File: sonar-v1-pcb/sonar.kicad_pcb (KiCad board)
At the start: 2 copper layers, 189 parts, among them U1 AD7606, U10 AD7606, U19 AD7606

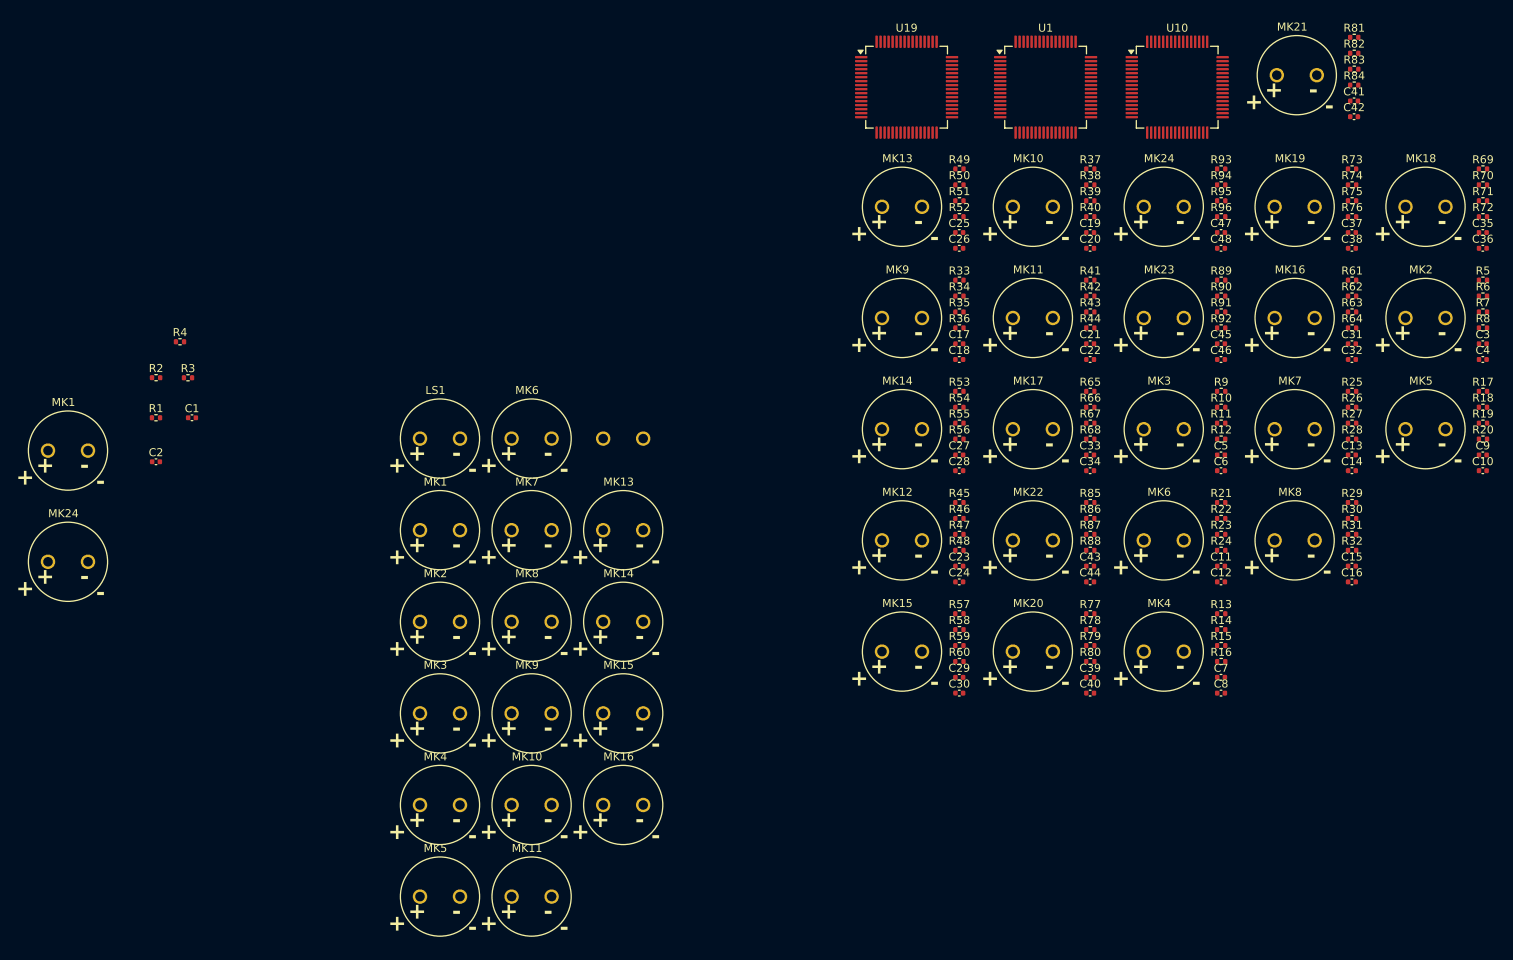
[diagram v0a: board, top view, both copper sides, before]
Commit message: Update gitignore and save schematic/PCB progress
Co-Authored-By: Claude Opus 4.6 <noreply@anthropic.com>
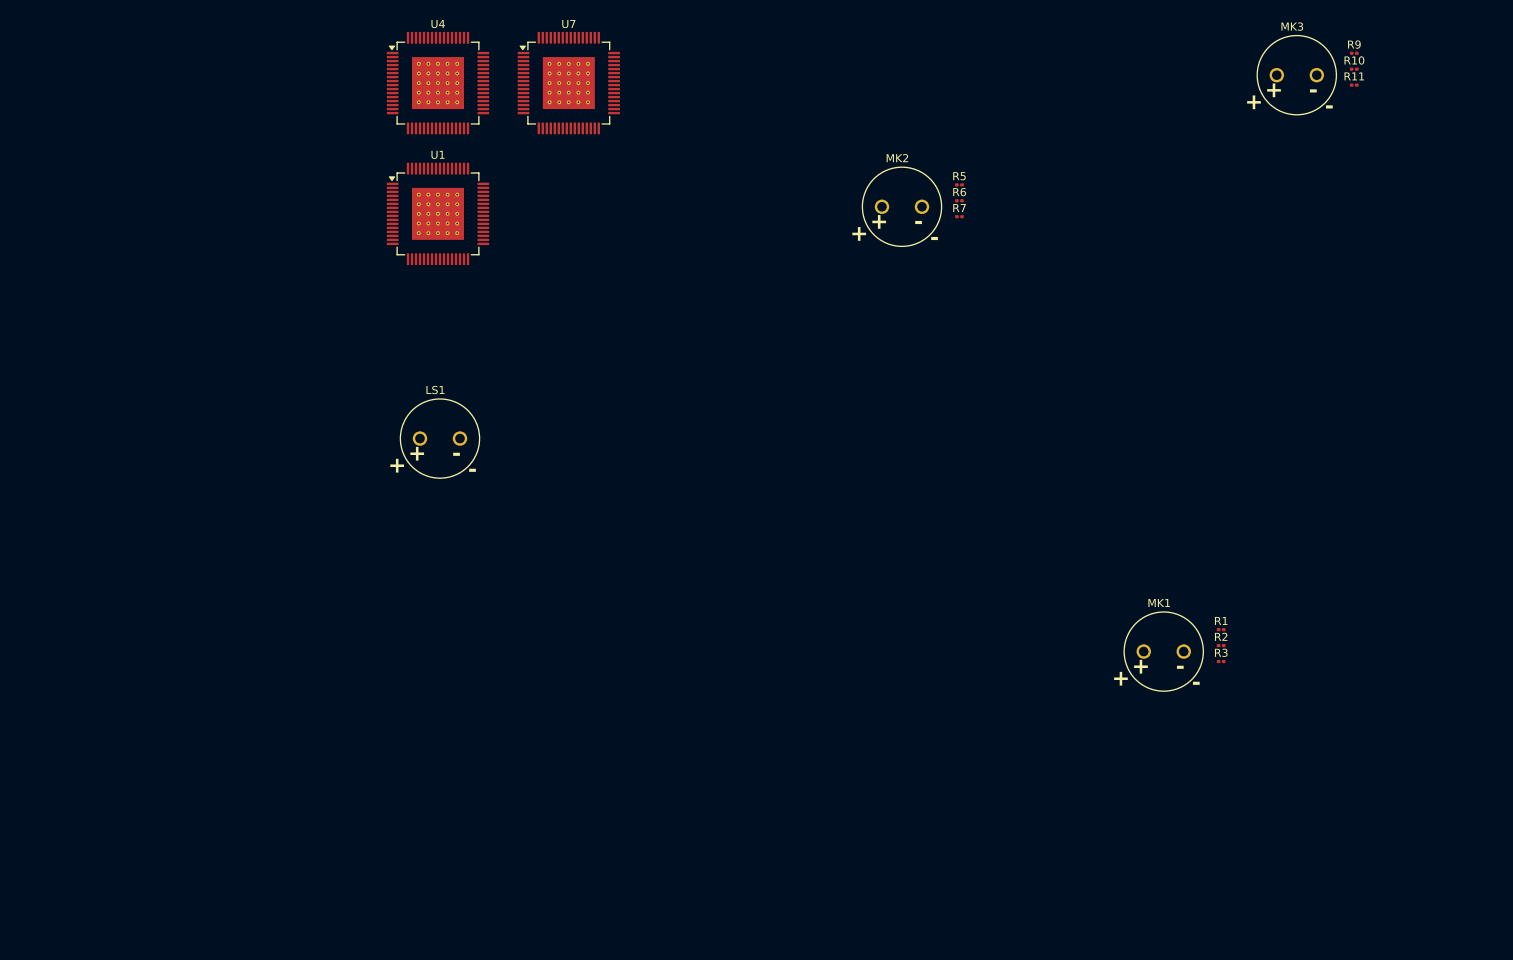
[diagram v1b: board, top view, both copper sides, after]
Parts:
- removed C1, C11, C13, C15, C17, C19, C21, C23, C25, C27, C29, C3, C31, C33, C35, C37, C39, C41, C43, C45, C47, C5, C7, C9: 100nF, Capacitor_SMD:C_0402_1005Metric
- removed C10, C12, C14, C16, C18, C2, C20, C22, C24, C26, C28, C30, C32, C34, C36, C38, C4, C40, C42, C44, C46, C48, C6, C8: 2.2nF, Capacitor_SMD:C_0402_1005Metric
- removed the MK1 at (117.5, 87.0)
- removed the MK1 at (71.0, 77.1)
- removed MK10 (x2), MK11 (x2), MK12 (x2), MK13, MK14 (x2), MK15 (x2), MK16 (x2), MK17, MK18, MK19, MK20, MK22, MK23, MK24 (x2), MK4, MK5 (x2), MK6 (x2), MK7 (x2), MK8 (x2), MK9 (x2): Microphone_Ultrasound, Sonar:MA40S4
- removed the MK2 at (117.5, 98.5)
- removed the MK2 at (240.7, 60.5)
- removed the MK3 at (117.5, 110.0)
- removed the MK3 at (208.0, 74.4)
- removed the R1 at (82.0, 73.0)
- removed the R10 at (215.2, 71.7)
- removed the R11 at (215.2, 73.7)
- removed R12, R20, R24, R28, R32, R36, R4, R40, R44, R48, R56, R60, R64, R68, R72, R76, R8, R80, R88, R92, R96: 1k, Resistor_SMD:R_0402_1005Metric
- removed R13, R17, R21, R25, R29, R33, R37, R41, R45, R49, R53, R57, R61, R65, R69, R73, R77, R81, R85, R89, R93: 1M, Resistor_SMD:R_0402_1005Metric
- removed R18, R22, R26, R30, R34, R38, R42, R46, R54, R58, R62, R66, R70, R74, R78, R86, R90, R94: 10k, Resistor_SMD:R_0402_1005Metric
- removed R19, R23, R27, R31, R35, R39, R43, R47, R55, R59, R63, R67, R71, R75, R79, R87, R91, R95: 290k, Resistor_SMD:R_0402_1005Metric
- removed the R2 at (82.0, 68.0)
- removed the R3 at (86.0, 68.0)
- removed the R5 at (247.9, 55.8)
- removed the R6 at (247.9, 57.8)
- removed the R7 at (247.9, 59.8)
- removed the R9 at (215.2, 69.7)
- removed U10, U19: AD7606, Package_QFP:LQFP-64_10x10mm_P0.5mm
- added U4: ADS8568SPM, Package_QFP:LQFP-64-1EP_10x10mm_P0.5mm_EP6.5x6.5mm_ThermalVias, F.Cu at (117.2, 31.2)
- added U7: ADS8568SPM, Package_QFP:LQFP-64-1EP_10x10mm_P0.5mm_EP6.5x6.5mm_ThermalVias, F.Cu at (133.6, 31.2)
- R1: renamed from R14; footprint Resistor_SMD:R_0402_1005Metric -> Capacitor_SMD:C_0201_0603Metric
- R10: renamed from R83; footprint Resistor_SMD:R_0402_1005Metric -> Capacitor_SMD:C_0201_0603Metric
- R11: renamed from R84; footprint Resistor_SMD:R_0402_1005Metric -> Capacitor_SMD:C_0201_0603Metric
- R2: renamed from R15; footprint Resistor_SMD:R_0402_1005Metric -> Capacitor_SMD:C_0201_0603Metric
- R3: renamed from R16; footprint Resistor_SMD:R_0402_1005Metric -> Capacitor_SMD:C_0201_0603Metric
- R5: renamed from R50; footprint Resistor_SMD:R_0402_1005Metric -> Capacitor_SMD:C_0201_0603Metric
- R6: renamed from R51; footprint Resistor_SMD:R_0402_1005Metric -> Capacitor_SMD:C_0201_0603Metric
- R7: renamed from R52; footprint Resistor_SMD:R_0402_1005Metric -> Capacitor_SMD:C_0201_0603Metric
- R9: renamed from R82; footprint Resistor_SMD:R_0402_1005Metric -> Capacitor_SMD:C_0201_0603Metric
- U1: value AD7606 -> ADS8568SPM; footprint Package_QFP:LQFP-64_10x10mm_P0.5mm -> Package_QFP:LQFP-64-1EP_10x10mm_P0.5mm_EP6.5x6.5mm_ThermalVias
- moved U1 77.6 mm to (117.2, 47.5)
- renumbered MK4 to MK1, MK13 to MK2, MK21 to MK3
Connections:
- MK1 pad 2: GND_RX -> /eight_transducer_array/10V
- MK2 pad 2: GND_RX -> /eight_transducer_array1/10V
- MK3 pad 2: GND_RX -> /eight_transducer_array2/10V
- R1 pad 2: GND_RX -> /eight_transducer_array/GND
- R11 pad 1: /eight_transducer_array2/RX_amp3/AMP_OUT -> Net-(U9--)
- R3 pad 1: /eight_transducer_array/RX_amp3/AMP_OUT -> Net-(U3--)
- R5 pad 2: GND_RX -> /eight_transducer_array1/GND
- R7 pad 1: /eight_transducer_array1/RX_amp3/AMP_OUT -> Net-(U6--)
- R9 pad 2: GND_RX -> /eight_transducer_array2/GND
- U1 pad 15: unconnected-(U1-FRSTDATA-Pad15) -> /eight_transducer_array/GND
- U1 pad 2: Net-(U1-AGND-Pad2) -> /eight_transducer_array/rx_amp.rx.7
- U1 pad 24: unconnected-(U1-DB7/DOUT_A-Pad24) -> /eight_transducer_array/GND
- U1 pad 26: Net-(U1-AGND-Pad2) -> unconnected-(U1-DB7-Pad26)
- U1 pad 35: Net-(U1-AGND-Pad2) -> unconnected-(U1-BUSY_INT-Pad35)
- U1 pad 37: unconnected-(U1-AVCC-Pad37) -> /eight_transducer_array/ADC_CONV_START
- U1 pad 38: unconnected-(U1-AVCC-Pad38) -> /eight_transducer_array/ADC_CONV_START
- U1 pad 39: unconnected-(U1-REGCAP-Pad39) -> /eight_transducer_array/ADC_CONV_START
- U1 pad 40: Net-(U1-AGND-Pad2) -> /eight_transducer_array/ADC_CONV_START
- U1 pad 41: Net-(U1-AGND-Pad2) -> unconnected-(U1-HW_SW_N-Pad41)
- U1 pad 42: unconnected-(U1-REFIN/REFOUT-Pad42) -> /eight_transducer_array/rx_amp.rx.0
- U1 pad 43: Net-(U1-REFGND-Pad43) -> unconnected-(U1-REFAP-Pad43)
- U1 pad 44: unconnected-(U1-REFCAPA-Pad44) -> /eight_transducer_array/GND
- U1 pad 46: Net-(U1-REFGND-Pad43) -> unconnected-(U1-REFAN-Pad46)
- U1 pad 47: Net-(U1-AGND-Pad2) -> /eight_transducer_array/rx_amp.rx.1
- U1 pad 49: /eight_transducer_array/RX_amp/AMP_OUT -> /eight_transducer_array/rx_amp.rx.2
- U1 pad 5: unconnected-(U1-OS2-Pad5) -> /eight_transducer_array/GND
- U1 pad 50: GND_RX -> unconnected-(U1-REFBP-Pad50)
- U1 pad 51: /eight_transducer_array/RX_amp5/AMP_OUT -> /eight_transducer_array/GND
- U1 pad 52: GND_RX -> unconnected-(U1-AVDD-Pad52)
- U1 pad 53: /eight_transducer_array/RX_amp1/AMP_OUT -> unconnected-(U1-REFBN-Pad53)
- U1 pad 54: GND_RX -> /eight_transducer_array/rx_amp.rx.3
- U1 pad 55: /eight_transducer_array/RX_amp6/AMP_OUT -> unconnected-(U1-REFN-Pad55)
- U1 pad 56: GND_RX -> unconnected-(U1-REFIO-Pad56)
- U1 pad 57: /eight_transducer_array/RX_amp2/AMP_OUT -> unconnected-(U1-AVDD-Pad57)
- U1 pad 58: GND_RX -> /eight_transducer_array/GND
- U1 pad 59: /eight_transducer_array/RX_amp7/AMP_OUT -> /eight_transducer_array/rx_amp.rx.5
- U1 pad 60: GND_RX -> unconnected-(U1-REFCN-Pad60)
- U1 pad 61: /eight_transducer_array/RX_amp3/AMP_OUT -> unconnected-(U1-AVDD-Pad61)
- U1 pad 62: GND_RX -> /eight_transducer_array/GND
- U1 pad 63: /eight_transducer_array/RX_amp4/AMP_OUT -> unconnected-(U1-REFCP-Pad63)
- U1 pad 64: GND_RX -> /eight_transducer_array/rx_amp.rx.4
- U1 pad 7: unconnected-(U1-~{STBY}-Pad7) -> /eight_transducer_array/rx_amp.rx.6
